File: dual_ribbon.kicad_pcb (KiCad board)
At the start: 2 copper layers, 100.5 x 101 mm, 54 parts, among them J1 Conn_01x02_Socket, J2 Conn_01x02_Socket, J3 Conn_01x02_Socket, J4 Conn_01x02_Socket, Q1 PNP, Q2 MMBF4391, Q3 MMBF4391, U1 LM4041LP-ADJ, U2 TL072, U3 OPA2134, U4 TL072, U5 TL072

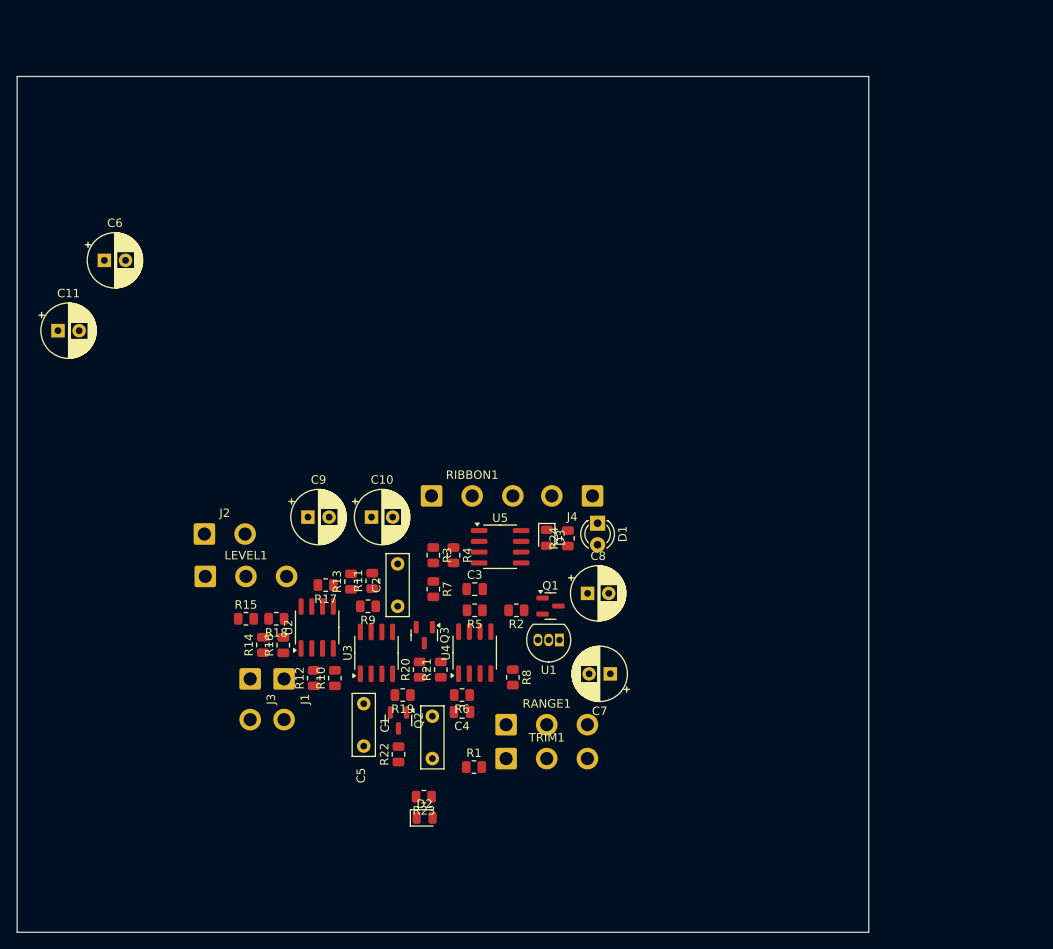
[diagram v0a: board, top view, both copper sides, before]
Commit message: Change parts to THT and do a test layout and route
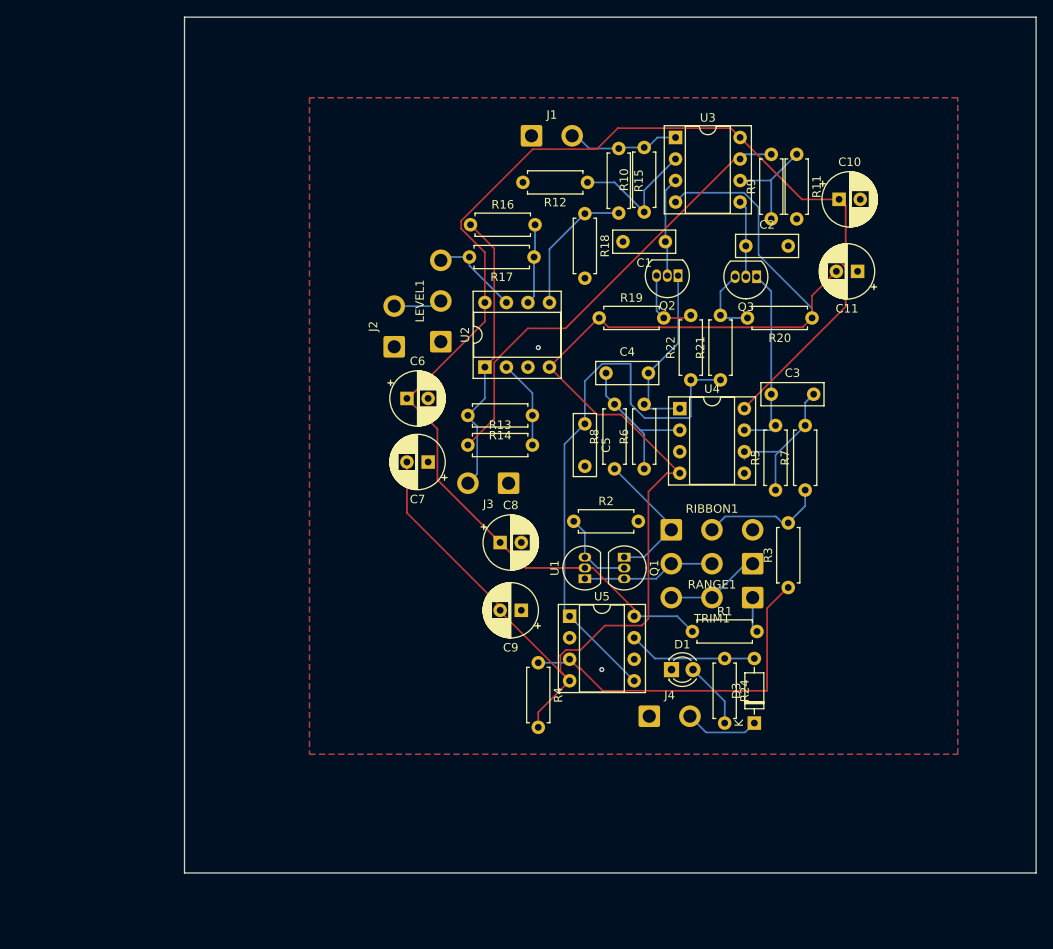
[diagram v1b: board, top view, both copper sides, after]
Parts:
- removed D2: 1N914, Diode_SMD:D_0805_2012Metric
- removed R23: 1k, Resistor_SMD:R_0805_2012Metric
- C3, C4: footprint Capacitor_SMD:C_0805_2012Metric -> Capacitor_THT:C_Rect_L7.2mm_W2.5mm_P5.00mm_FKS2_FKP2_MKS2_MKP2
- D3: footprint Diode_SMD:D_0805_2012Metric -> Diode_THT:D_DO-35_SOD27_P7.62mm_Horizontal
- Q1, Q2, Q3: footprint Package_TO_SOT_SMD:SOT-23 -> Package_TO_SOT_THT:TO-92_Inline
- R1, R10, R11, R12, R13, R14, R15, R16, R17, R18, R19, R2, R20, R21, R22, R24, R3, R4, R5, R6, R7, R8, R9: footprint Resistor_SMD:R_0805_2012Metric -> Resistor_THT:R_Axial_DIN0207_L6.3mm_D2.5mm_P7.62mm_Horizontal
- U2, U3, U4, U5: footprint Package_SO:SOIC-8_3.9x4.9mm_P1.27mm -> Package_DIP:DIP-8_W7.62mm_Socket
- moved C11 94.6 mm to (190.2, 68.5), turned to 180 degrees
- moved R11 71.0 mm to (183.0, 54.7), turned to -90 degrees
- moved R15 70.8 mm to (162.0, 54.0), turned to -90 degrees
- moved J1 70.4 mm to (151.7, 52.5), turned to 0 degrees
- moved U3 70.3 mm to (168.7, 52.7), turned to 0 degrees
- moved R12 66.8 mm to (158.3, 58.0), turned to 180 degrees
- moved C10 66.7 mm to (188.0, 60.0)
- moved R10 66.0 mm to (165.0, 61.5)
- moved R9 66.0 mm to (180.0, 62.3), turned to 90 degrees
- moved C1 65.1 mm to (167.5, 65.0), turned to 180 degrees
- moved R20 62.2 mm to (184.8, 74.0), turned to 180 degrees
- moved Q2 62.0 mm to (169.0, 69.0), turned to 180 degrees
- moved R18 60.1 mm to (158.0, 61.7), turned to -90 degrees
- moved C2 59.1 mm to (177.0, 65.5), turned to 0 degrees
- moved Q3 57.7 mm to (178.3, 69.1), turned to 180 degrees
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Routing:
- net -12V: track 0.00 -> 164.2 mm
- net +12V: track 0.00 -> 161.1 mm
- net Net-(D2-K): track 0.00 -> 66.4 mm
- net Net-(R13-Pad1): track 0.00 -> 53.9 mm
- net Net-(U5A-+): track 0.00 -> 42.0 mm
- net Net-(J3-Pin_2): track 0.00 -> 33.9 mm
- net Net-(Q3-D): track 0.00 -> 22.4 mm
- net Net-(Q2-D): track 0.00 -> 21.3 mm
- net Net-(U4B--): track 0.00 -> 18.2 mm
- net Net-(U4A--): track 0.00 -> 17.8 mm
- net Net-(Q1-C): track 0.00 -> 16.9 mm
- net Net-(U2B-+): track 0.00 -> 16.3 mm
- net Net-(U3A--): track 0.00 -> 15.9 mm
- net Net-(Q1-E): track 0.00 -> 15.7 mm
- net Net-(D3-A): track 0.00 -> 15.2 mm
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- added copper zone on B.Cu, net GND
- added copper zone on F.Cu, net GND

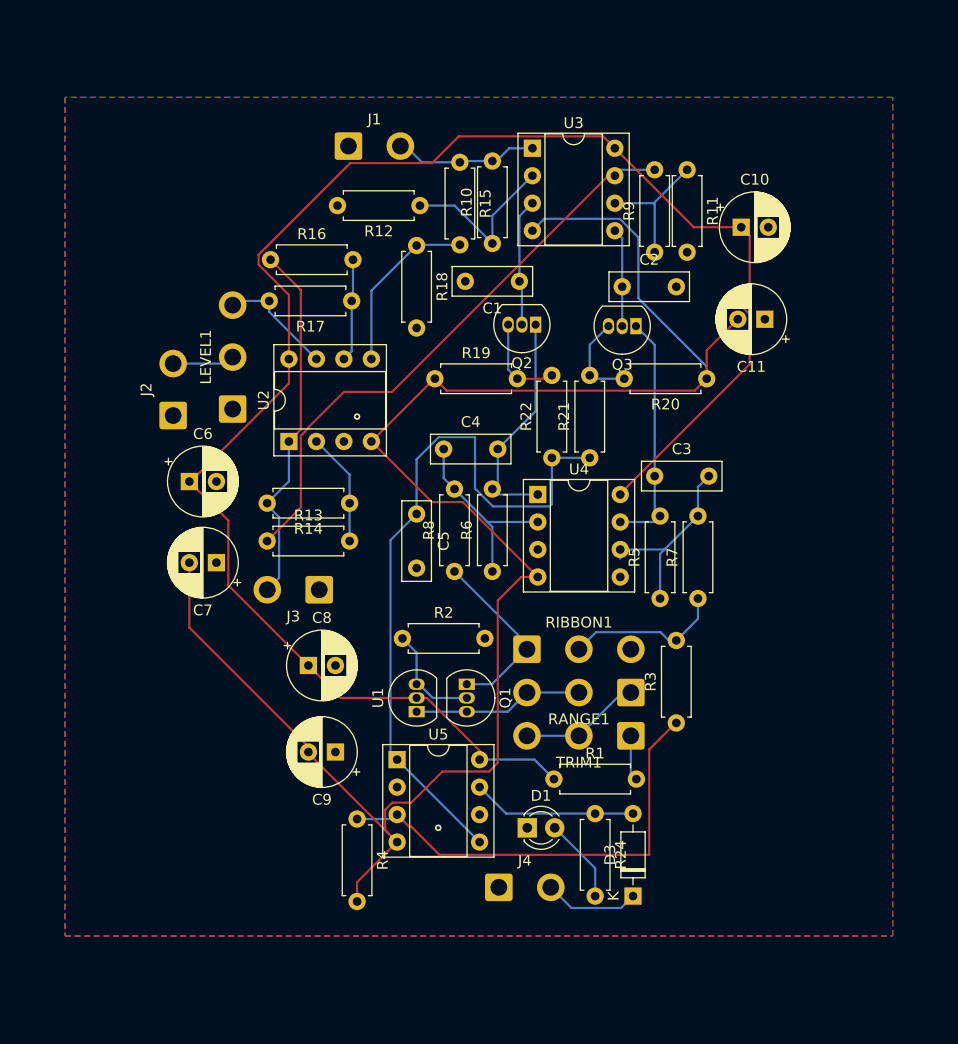
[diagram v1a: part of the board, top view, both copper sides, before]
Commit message: Redid the routing
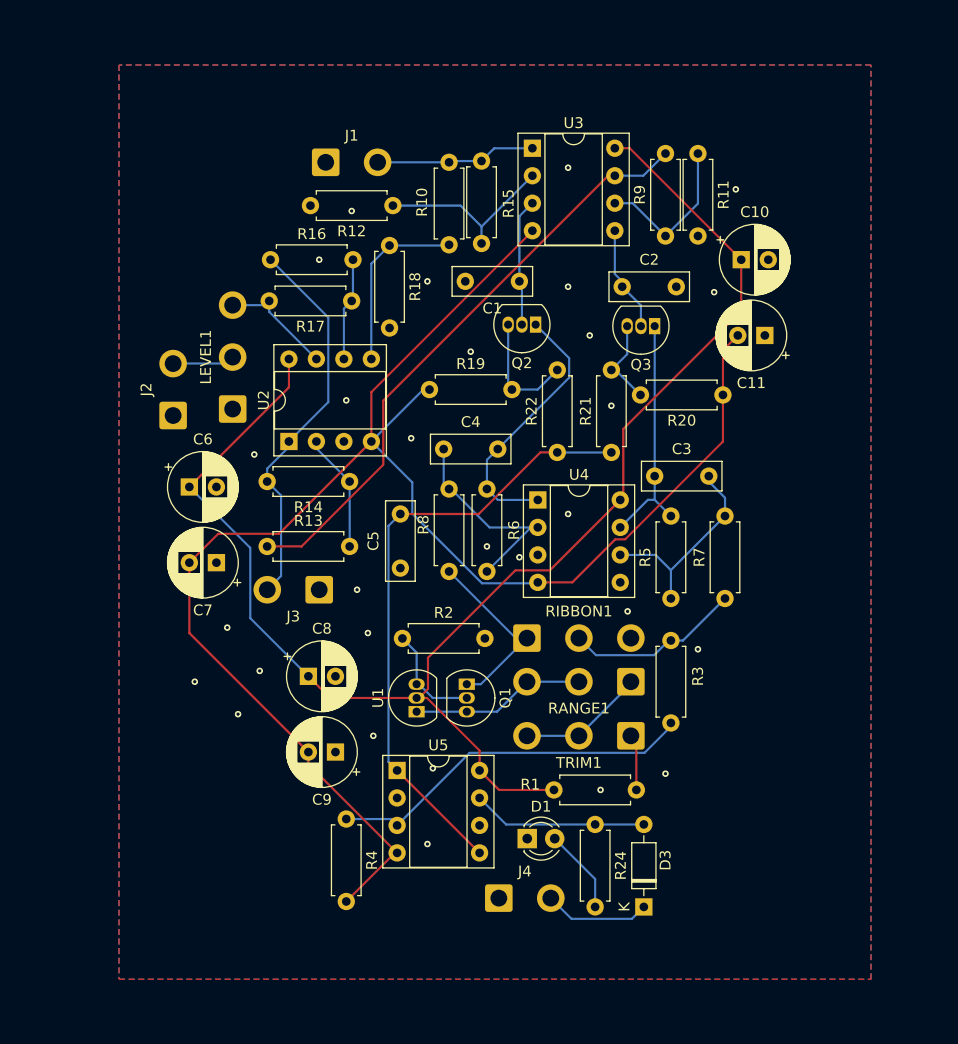
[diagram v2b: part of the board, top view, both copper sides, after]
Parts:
- moved C10 3.00 mm to (188.0, 63.0)
- moved J1 2.58 mm to (149.6, 54.0)
- moved R12 2.50 mm to (155.8, 58.0)
- moved R18 2.50 mm to (155.5, 61.7)
- moved R7 2.50 mm to (186.5, 94.3)
- moved R20 2.12 mm to (186.3, 75.5)
- moved R21 2.06 mm to (176.0, 80.8)
- moved R14 2.00 mm to (151.8, 83.5)
- moved R11 1.80 mm to (184.0, 53.2)
- moved R9 1.80 mm to (181.0, 60.8)
- moved Q3 1.73 mm to (180.0, 69.1)
- moved C11 1.50 mm to (190.2, 70.0)
- moved C5 1.50 mm to (156.5, 86.5)
- moved D3 1.41 mm to (179.0, 122.8)
- moved R19 1.12 mm to (159.2, 75.0)
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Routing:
- net +12V: track 161.1 -> 136.7 mm
- net -12V: track 164.2 -> 151.2 mm
- net Net-(D2-K): track 66.4 -> 57.1 mm
- net Net-(U5A-+): track 42.0 -> 34.4 mm
- net Net-(Q2-D): track 21.3 -> 24.7 mm
- net Net-(Q2-G): track 8.67 -> 11.1 mm
- net Net-(U3B--): track 12.5 -> 14.8 mm
- net Net-(J3-Pin_2): track 33.9 -> 36.1 mm
- net Net-(U4A--): track 17.8 -> 20.0 mm
- net Net-(R3-Pad2): track 14.7 -> 16.3 mm
- net Net-(J1-Pin_2): track 13.4 -> 14.8 mm
- net Net-(R13-Pad1): track 53.9 -> 55.3 mm
- net Net-(U3A--): track 15.9 -> 17.2 mm
- net Net-(U4B--): track 18.2 -> 19.3 mm
- net Net-(D3-K): track 8.85 -> 9.85 mm
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
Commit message: Do gerbers
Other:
- board size 100.5 x 101 mm -> 100 x 100 mm
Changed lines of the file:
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@@
 			(outputformat 1)
 			(mirror no)
-			(drillshape 1)
+			(drillshape 0)
 			(scaleselection 1)
-			(outputdirectory "")
+			(outputdirectory "C:/Users/nolan.greig/Documents/flerb/")
 		)
 	)
@@
 	(gr_rect
 		(start 110.75 38.5)
-		(end 211.25 139.5)
+		(end 210.75 138.5)
 		(stroke
 			(width 0.05)

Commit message: Schematic cleanup and placement
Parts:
- added C12: 22n, Capacitor_THT:C_Disc_D3.0mm_W2.0mm_P2.50mm, F.Cu at (160.0, 94.7)
- added C13: 4.7u, Capacitor_THT:C_Radial_D6.3mm_H5.0mm_P2.50mm, F.Cu at (168.2, 78.5)
- added C14: 22n, Capacitor_THT:C_Disc_D3.0mm_W2.0mm_P2.50mm, F.Cu at (176.0, 87.9)
- added D10: 1N4148, Diode_THT:D_DO-35_SOD27_P7.62mm_Horizontal, F.Cu at (97.2, 44.0)
- added D11: LED, LED_THT:LED_D3.0mm, F.Cu at (112.6, 108.0)
- added D4: 1N4148, Diode_THT:D_DO-35_SOD27_P7.62mm_Horizontal, F.Cu at (149.8, 93.0)
- added D5: 1N1418, Diode_THT:D_DO-35_SOD27_P7.62mm_Horizontal, F.Cu at (23.2, 54.5)
- added D6: 5.1V, Diode_THT:D_DO-35_SOD27_P7.62mm_Horizontal, F.Cu at (25.5, 134.5)
- added D7: 5.1V, Diode_THT:D_DO-35_SOD27_P7.62mm_Horizontal, F.Cu at (25.7, 138.5)
- added D8: 1N4148, Diode_THT:D_DO-35_SOD27_P7.62mm_Horizontal, F.Cu at (36.8, 132.0)
- added D9: 1N4148, Diode_THT:D_DO-35_SOD27_P7.62mm_Horizontal, F.Cu at (25.5, 130.5)
- added J10: LFO OUT, Connector_Wire:SolderWire-0.75sqmm_1x02_P4.8mm_D1.25mm_OD2.3mm, F.Cu at (29.1, 102.0)
- added J11: OUT, Connector_Wire:SolderWire-0.75sqmm_1x02_P4.8mm_D1.25mm_OD2.3mm, F.Cu at (67.2, 79.8)
- added J5: GATE IN, Connector_Wire:SolderWire-0.75sqmm_1x02_P4.8mm_D1.25mm_OD2.3mm, F.Cu at (134.0, 99.0)
- added J6: AR OUT, Connector_Wire:SolderWire-0.75sqmm_1x02_P4.8mm_D1.25mm_OD2.3mm, F.Cu at (87.6, 39.0)
- added J7: SQUARE OUT, Connector_Wire:SolderWire-0.75sqmm_1x02_P4.8mm_D1.25mm_OD2.3mm, F.Cu at (190.5, 88.7)
- added J8: TRI OUT, Connector_Wire:SolderWire-0.75sqmm_1x02_P4.8mm_D1.25mm_OD2.3mm, F.Cu at (181.8, 82.2)
- added J9: SINE OUT, Connector_Wire:SolderWire-0.75sqmm_1x02_P4.8mm_D1.25mm_OD2.3mm, F.Cu at (67.2, 70.5)
- added Q4: MMBF4391, Package_TO_SOT_THT:TO-92_Inline, F.Cu at (133.0, 92.8)
- added Q5: 2N3906, Package_TO_SOT_THT:TO-92_Inline, F.Cu at (138.4, 91.3)
- added Q6: 2N3904, Package_TO_SOT_THT:TO-92_Inline, F.Cu at (120.9, 107.6)
- added R25: 10k, Resistor_THT:R_Axial_DIN0207_L6.3mm_D2.5mm_P7.62mm_Horizontal, F.Cu at (149.8, 90.0)
- added R26: 200k, Resistor_THT:R_Axial_DIN0207_L6.3mm_D2.5mm_P7.62mm_Horizontal, F.Cu at (134.0, 87.0)
- added R27: 91k, Resistor_THT:R_Axial_DIN0207_L6.3mm_D2.5mm_P7.62mm_Horizontal, F.Cu at (43.5, 141.0)
- added R28: 30k, Resistor_THT:R_Axial_DIN0207_L6.3mm_D2.5mm_P7.62mm_Horizontal, F.Cu at (36.2, 146.5)
- added R29: 10k, Resistor_THT:R_Axial_DIN0207_L6.3mm_D2.5mm_P7.62mm_Horizontal, F.Cu at (138.0, 85.8)
- added R30: 1M, Resistor_THT:R_Axial_DIN0207_L6.3mm_D2.5mm_P7.62mm_Horizontal, F.Cu at (128.5, 91.7)
- added R31: 47k, Resistor_THT:R_Axial_DIN0207_L6.3mm_D2.5mm_P7.62mm_Horizontal, F.Cu at (23.2, 76.1)
- added R32: 1M, Resistor_THT:R_Axial_DIN0207_L6.3mm_D2.5mm_P7.62mm_Horizontal, F.Cu at (30.7, 80.0)
- added R33: 1k, Resistor_THT:R_Axial_DIN0207_L6.3mm_D2.5mm_P7.62mm_Horizontal, F.Cu at (35.9, 135.5)
- added R34: 39k, Resistor_THT:R_Axial_DIN0207_L6.3mm_D2.5mm_P7.62mm_Horizontal, F.Cu at (161.8, 98.2)
- added R35: 3k, Resistor_THT:R_Axial_DIN0207_L6.3mm_D2.5mm_P7.62mm_Horizontal, F.Cu at (104.8, 49.0)
- added R36: 47k, Resistor_THT:R_Axial_DIN0207_L6.3mm_D2.5mm_P7.62mm_Horizontal, F.Cu at (34.0, 55.9)
- added R37: 220, Resistor_THT:R_Axial_DIN0207_L6.3mm_D2.5mm_P7.62mm_Horizontal, F.Cu at (34.0, 59.9)
- added R38: 47k, Resistor_THT:R_Axial_DIN0207_L6.3mm_D2.5mm_P7.62mm_Horizontal, F.Cu at (185.8, 97.7)
- added R39: 100k, Resistor_THT:R_Axial_DIN0207_L6.3mm_D2.5mm_P7.62mm_Horizontal, F.Cu at (186.0, 90.7)
- added R40: 5.6k, Resistor_THT:R_Axial_DIN0207_L6.3mm_D2.5mm_P7.62mm_Horizontal, F.Cu at (178.4, 94.2)
- added R41: 4.7k, Resistor_THT:R_Axial_DIN0207_L6.3mm_D2.5mm_P7.62mm_Horizontal, F.Cu at (178.4, 87.2)
- added R42: 1.8k, Resistor_THT:R_Axial_DIN0207_L6.3mm_D2.5mm_P7.62mm_Horizontal, F.Cu at (100.5, 97.5)
- added R43: 100k, Resistor_THT:R_Axial_DIN0207_L6.3mm_D2.5mm_P7.62mm_Horizontal, F.Cu at (109.4, 102.5)
- added R44: 56k, Resistor_THT:R_Axial_DIN0207_L6.3mm_D2.5mm_P7.62mm_Horizontal, F.Cu at (92.7, 94.5)
- added R45: 18k, Resistor_THT:R_Axial_DIN0207_L6.3mm_D2.5mm_P7.62mm_Horizontal, F.Cu at (44.8, 51.8)
- added R46: 4.k, Resistor_THT:R_Axial_DIN0207_L6.3mm_D2.5mm_P7.62mm_Horizontal, F.Cu at (44.8, 55.9)
- added R47: 15k, Resistor_THT:R_Axial_DIN0207_L6.3mm_D2.5mm_P7.62mm_Horizontal, F.Cu at (44.8, 59.9)
- added R48: 100k, Resistor_THT:R_Axial_DIN0207_L6.3mm_D2.5mm_P7.62mm_Horizontal, F.Cu at (44.8, 64.0)
- added R49: 3k, Resistor_THT:R_Axial_DIN0207_L6.3mm_D2.5mm_P7.62mm_Horizontal, F.Cu at (44.8, 68.0)
- added R50: 200k, Resistor_THT:R_Axial_DIN0207_L6.3mm_D2.5mm_P7.62mm_Horizontal, F.Cu at (44.8, 72.1)
- added R51: 1k, Resistor_THT:R_Axial_DIN0207_L6.3mm_D2.5mm_P7.62mm_Horizontal, F.Cu at (44.8, 76.1)
- added R52: 200k, Resistor_THT:R_Axial_DIN0207_L6.3mm_D2.5mm_P7.62mm_Horizontal, F.Cu at (69.7, 99.5)
- added R53: 47k, Resistor_THT:R_Axial_DIN0207_L6.3mm_D2.5mm_P7.62mm_Horizontal, F.Cu at (69.7, 103.5)
- added R54: 47k, Resistor_THT:R_Axial_DIN0207_L6.3mm_D2.5mm_P7.62mm_Horizontal, F.Cu at (77.0, 106.5)
- added R55: 47k, Resistor_THT:R_Axial_DIN0207_L6.3mm_D2.5mm_P7.62mm_Horizontal, F.Cu at (154.7, 85.5)
- added R56: 7.5k, Resistor_THT:R_Axial_DIN0207_L6.3mm_D2.5mm_P7.62mm_Horizontal, F.Cu at (109.2, 63.5)
- added R57: 100k, Resistor_THT:R_Axial_DIN0207_L6.3mm_D2.5mm_P7.62mm_Horizontal, F.Cu at (55.5, 59.9)
- added R58: 10k, Resistor_THT:R_Axial_DIN0207_L6.3mm_D2.5mm_P7.62mm_Horizontal, F.Cu at (125.5, 99.3)
- added R59: 3k, Resistor_THT:R_Axial_DIN0207_L6.3mm_D2.5mm_P7.62mm_Horizontal, F.Cu at (55.5, 68.0)
- added R60: 100k, Resistor_THT:R_Axial_DIN0207_L6.3mm_D2.5mm_P7.62mm_Horizontal, F.Cu at (119.9, 102.5)
- added R61: 3.9k, Resistor_THT:R_Axial_DIN0207_L6.3mm_D2.5mm_P7.62mm_Horizontal, F.Cu at (131.1, 108.0)
- added RV1: 1M, Connector_Wire:SolderWire-0.75sqmm_1x03_P4.8mm_D1.25mm_OD2.3mm, F.Cu at (84.9, 56.0)
- added RV2: 1M, Connector_Wire:SolderWire-0.75sqmm_1x03_P4.8mm_D1.25mm_OD2.3mm, F.Cu at (84.9, 60.6)
- added RV3: 100k, Connector_Wire:SolderWire-0.75sqmm_1x03_P4.8mm_D1.25mm_OD2.3mm, F.Cu at (84.9, 65.2)
- added RV4: 100k, Connector_Wire:SolderWire-0.75sqmm_1x03_P4.8mm_D1.25mm_OD2.3mm, F.Cu at (84.9, 69.8)
- added RV5: 100k, Connector_Wire:SolderWire-0.75sqmm_1x03_P4.8mm_D1.25mm_OD2.3mm, F.Cu at (63.0, 94.5)
- added RV6: 100k, Connector_Wire:SolderWire-0.75sqmm_1x03_P4.8mm_D1.25mm_OD2.3mm, F.Cu at (84.9, 79.0)
- added SW1: SW_SP3T, Connector_Wire:SolderWire-0.75sqmm_1x04_P4.8mm_D1.25mm_OD2.3mm, F.Cu at (81.8, 162.5)
- added SW2: GATE/TRIG, Connector_Wire:SolderWire-0.75sqmm_1x04_P4.8mm_D1.25mm_OD2.3mm, F.Cu at (129.9, 81.0)
- added U6: TL074, Package_DIP:DIP-14_W7.62mm_Socket, F.Cu at (165.4, 85.4)
- added U7: TL072, Package_DIP:DIP-8_W7.62mm_Socket, F.Cu at (75.7, 130.2)
- added U8: LM13700, Package_DIP:DIP-16_W7.62mm_Socket, F.Cu at (81.0, 94.4)
- J1: value Conn_01x02_Socket -> HIGH OUT
- J2: value Conn_01x02_Socket -> DIFF OUT
- J3: value Conn_01x02_Socket -> LOW OUT
- J4: value Conn_01x02_Socket -> GATE OUT
- moved C11 83.0 mm to (273.2, 70.0)
- moved C1 83.0 mm to (250.5, 65.0)
- moved C10 83.0 mm to (271.0, 63.0)
- moved C2 83.0 mm to (260.0, 65.5)
- moved C3 83.0 mm to (263.0, 83.0)
- moved C4 83.0 mm to (243.5, 80.5)
- moved C5 83.0 mm to (239.5, 86.5)
- moved C6 83.0 mm to (220.0, 84.0)
- moved C7 83.0 mm to (222.5, 91.0)
- moved C8 83.0 mm to (231.0, 101.5)
- moved C9 83.0 mm to (233.5, 108.5)
- moved D1 83.0 mm to (251.2, 116.5)
- moved D3 83.0 mm to (262.0, 122.8)
- moved J1 83.0 mm to (232.6, 54.0)
- moved J2 83.0 mm to (218.5, 77.4)
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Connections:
- net Net-(D3-A) renamed GATE
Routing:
- net -12V: track 151.2 -> 0.00 mm
- net +12V: track 136.7 -> 0.00 mm
- net Net-(D2-K): track 57.1 -> 0.00 mm
- net Net-(R13-Pad1): track 55.3 -> 0.00 mm
- net Net-(J3-Pin_2): track 36.1 -> 0.00 mm
- net Net-(U5A-+): track 34.4 -> 0.00 mm
- net Net-(Q2-D): track 24.7 -> 0.00 mm
- net Net-(Q3-D): track 22.4 -> 0.00 mm
- net Net-(U4A--): track 20.0 -> 0.00 mm
- net Net-(U4B--): track 19.3 -> 0.00 mm
- net Net-(U3A--): track 17.2 -> 0.00 mm
- net Net-(Q1-C): track 17.1 -> 0.00 mm
- net Net-(U2B-+): track 16.7 -> 0.00 mm
- net Net-(R3-Pad2): track 16.3 -> 0.00 mm
- net GATE: track 16.2 -> 0.00 mm
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- removed copper zone on B.Cu, net GND
- removed copper zone on F.Cu, net GND

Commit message: Did the combined layout
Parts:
- moved R46 194.8 mm to (223.6, 133.0), turned to 180 degrees
- moved R45 194.7 mm to (223.3, 129.5), turned to 180 degrees
- moved R36 193.4 mm to (226.8, 70.5), turned to 180 degrees
- moved R47 190.4 mm to (223.3, 126.0), turned to 180 degrees
- moved R31 188.3 mm to (210.5, 56.7), turned to -90 degrees
- moved R32 184.0 mm to (214.0, 64.3), turned to 90 degrees
- moved D5 180.4 mm to (202.5, 74.3), turned to 180 degrees
- moved R48 179.0 mm to (219.8, 101.5), turned to 180 degrees
- moved R28 175.6 mm to (194.9, 71.3)
- moved D9 175.2 mm to (194.7, 85.0)
- moved R33 175.2 mm to (202.5, 81.5), turned to 180 degrees
- moved D7 174.8 mm to (194.7, 94.0)
- moved D6 174.7 mm to (194.7, 91.0)
- moved R37 173.0 mm to (207.0, 56.7), turned to -90 degrees
- moved D8 171.2 mm to (202.3, 88.0), turned to 180 degrees
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
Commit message: Did routing
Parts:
- moved J5 35.3 mm to (247.7, 135.0)
- moved D1 11.9 mm to (257.0, 134.5)
- moved J4 10.1 mm to (264.2, 135.0)
- moved D3 3.10 mm to (267.8, 131.3)
- moved R1 3.10 mm to (259.5, 120.5)
- moved R24 3.10 mm to (263.3, 123.7)
- moved RV1 1.10 mm to (183.5, 71.0)
- moved R29 0.31 mm to (232.4, 92.0)
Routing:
- net +12V: track 0.00 -> 359.3 mm
- net -12V: track 0.00 -> 348.0 mm
- net Net-(J8-Pin_2): track 0.00 -> 119.4 mm
- net Net-(J9-Pin_2): track 0.00 -> 114.7 mm
- net Net-(D5-K): track 0.00 -> 97.8 mm
- net Net-(J7-Pin_2): track 0.00 -> 95.9 mm
- net Net-(U7A-+): track 0.00 -> 74.1 mm
- net Net-(J3-Pin_2): track 0.00 -> 65.3 mm
- net Net-(R47-Pad1): track 0.00 -> 63.8 mm
- net Net-(U6A-+): track 0.00 -> 63.5 mm
- net Net-(Q4-S): track 0.00 -> 60.6 mm
- net Net-(R54-Pad2): track 0.00 -> 60.3 mm
- net Net-(D2-K): track 0.00 -> 57.3 mm
- net Net-(R39-Pad2): track 0.00 -> 55.6 mm
- net Net-(R55-Pad1): track 0.00 -> 53.8 mm
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- added copper zone on B.Cu, net GND
- added copper zone on F.Cu, net GND
